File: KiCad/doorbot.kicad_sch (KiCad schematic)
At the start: 54 parts, among them J1 SERVO, J10 Raspberry_Pi_2_3, J2 POWER, J3 SIEDLE LED, J4 SIEDLE KEY, J5 ERT SWITCH, J6 ERT SIEDLE, J7 BUZZER, J8 UI LED, J9 UI BUTTON, Q1 BC337, Q2 BC548, Q3 BC548, U1 PC817, U2 PC817, U3 74HC14, U4 EPR211A064, U5 EPR211A064, U6 L4940, U7 MIC29302WT

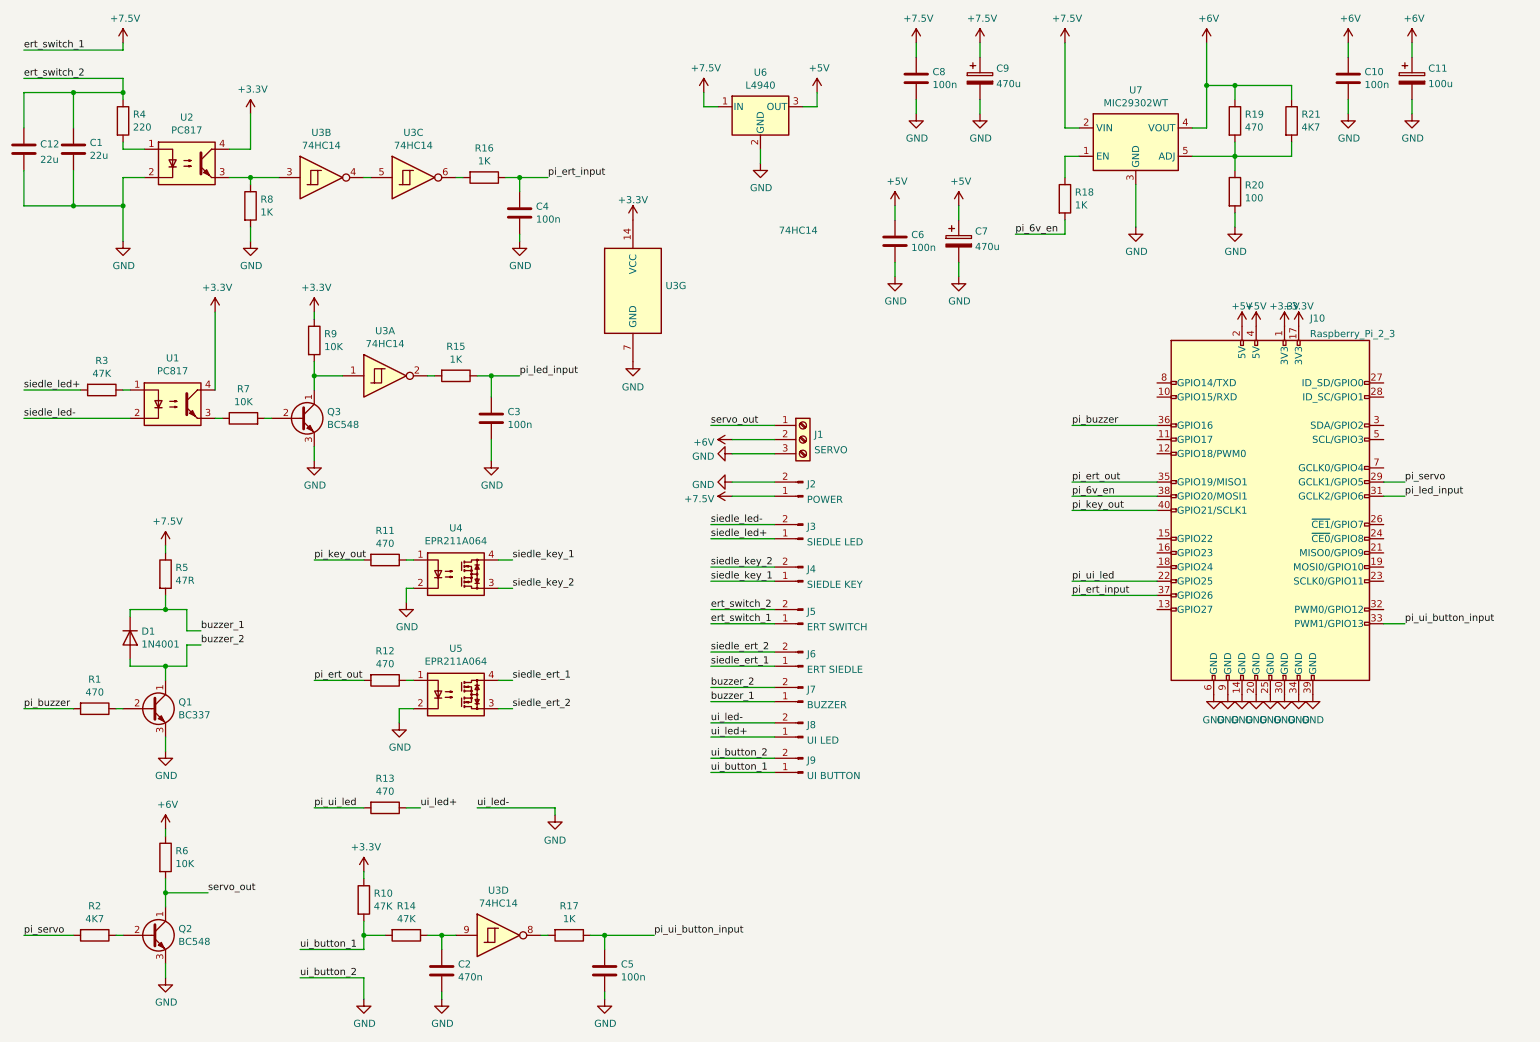
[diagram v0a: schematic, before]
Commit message: Route the stripboard PCB
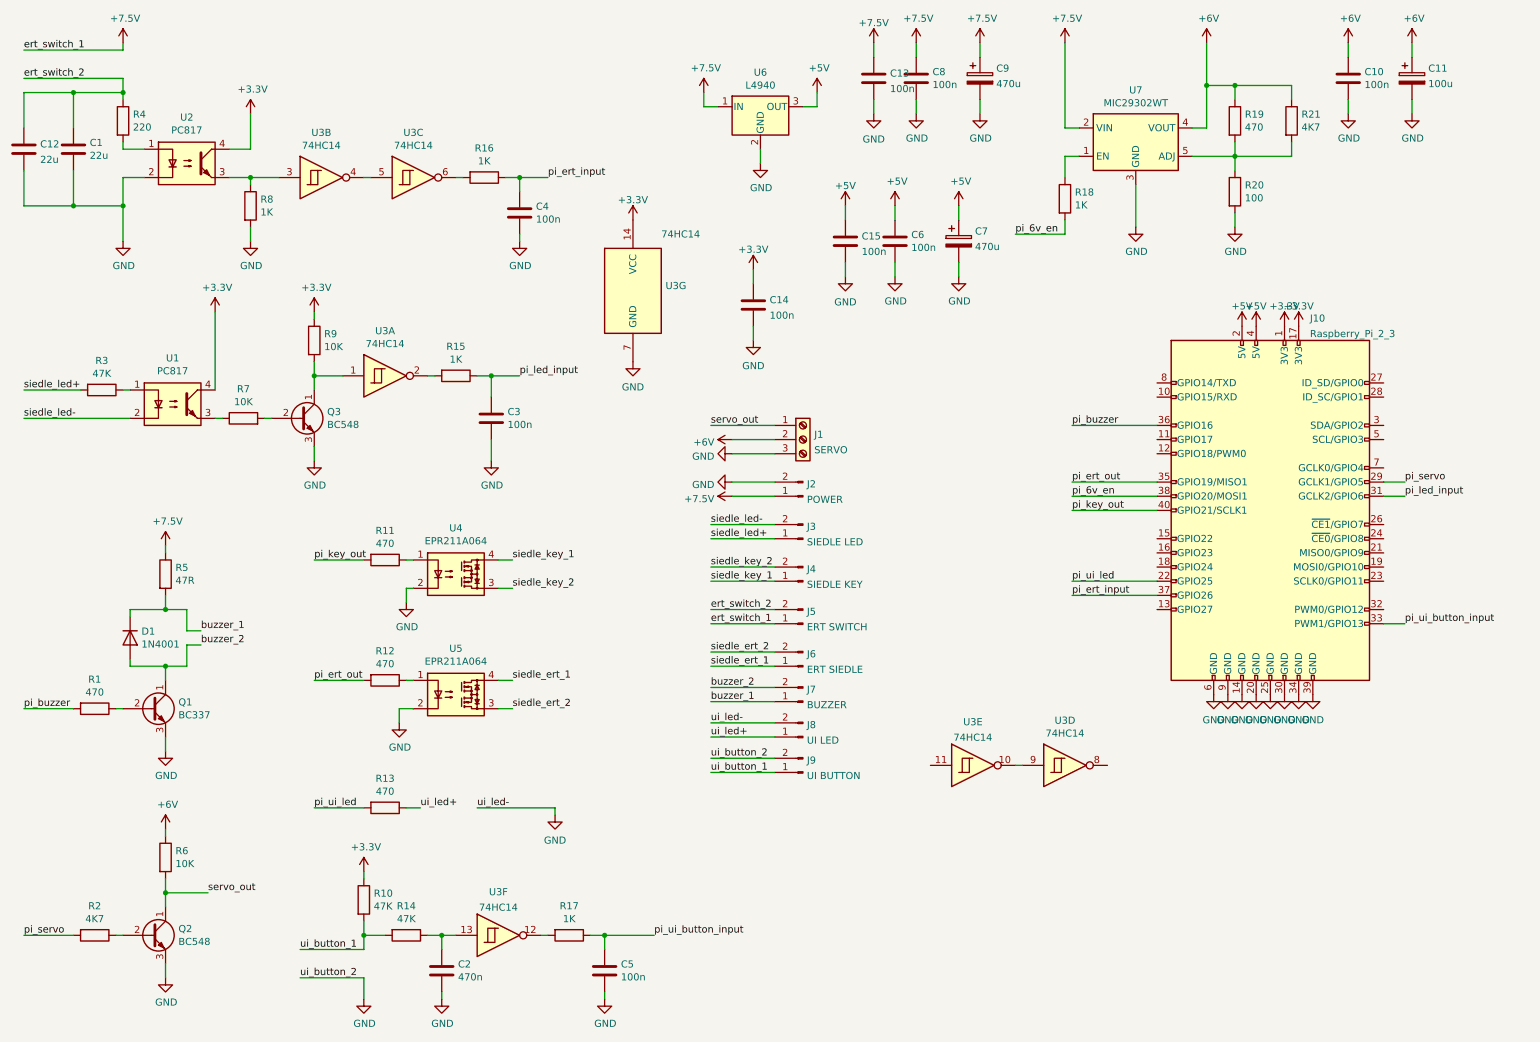
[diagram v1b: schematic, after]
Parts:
- added C13, C14, C15: 100n, Capacitor_THT:C_Disc_D5.0mm_W2.5mm_P2.50mm, symbol Device:C
- added unit 6 of U3
- added unit 5 of U3
- D1: footprint Diode_THT:D_DO-41_SOD81_P10.16mm_Horizontal -> Diode_THT:D_DO-41_SOD81_P2.54mm_Vertical_AnodeUp
- Q1, Q2, Q3: footprint Package_TO_SOT_THT:TO-92_Inline -> Package_TO_SOT_THT:TO-92_Inline_Wide
- R1, R17, R19, R2, R21, R4, R6: footprint Resistor_THT:R_Axial_DIN0207_L6.3mm_D2.5mm_P10.16mm_Horizontal -> Resistor_THT:R_Axial_DIN0207_L6.3mm_D2.5mm_P2.54mm_Vertical
- R10, R15: footprint Resistor_THT:R_Axial_DIN0207_L6.3mm_D2.5mm_P10.16mm_Horizontal -> Resistor_THT:R_Axial_DIN0309_L9.0mm_D3.2mm_P12.70mm_Horizontal
- R11, R13, R14, R18, R20, R3, R5: footprint Resistor_THT:R_Axial_DIN0207_L6.3mm_D2.5mm_P10.16mm_Horizontal -> Resistor_THT:R_Axial_DIN0207_L6.3mm_D2.5mm_P5.08mm_Vertical
- R16: footprint Resistor_THT:R_Axial_DIN0207_L6.3mm_D2.5mm_P10.16mm_Horizontal -> Resistor_THT:R_Axial_DIN0207_L6.3mm_D2.5mm_P15.24mm_Horizontal
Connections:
- net +3V3: now also C14.1
- net +5V: now also C15.1
- net +7.5V: now also C13.1
- net GND: now also C13.2, C14.2, C15.2
- net at C2.1, R14.1: now also U3.13; no longer U3.9
- net at U3.8: no longer R17.2
- new net: U3.10, U3.9
- new net: R17.2, U3.12
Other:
- moved on the sheet: U3D

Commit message: Add the final PCB version
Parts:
- added FB1: Bead, Resistor_THT:R_Axial_DIN0207_L6.3mm_D2.5mm_P10.16mm_Horizontal, symbol Device:FerriteBead
- C12: renamed from C7; value 470u -> 2200u 10V
- C13: renamed from C9; value 470u -> 1000u 16V
- C7: renamed from C14; footprint Capacitor_THT:C_Disc_D5.0mm_W2.5mm_P2.50mm -> Capacitor_THT:C_Disc_D7.5mm_W5.0mm_P7.50mm
- renumbered C12 to C1, C6 to C10, C8 to C11, C10 to C14, C11 to C15, C1 to C2, C2 to C3, C3 to C4, C4 to C5, C5 to C6, C15 to C8, C13 to C9
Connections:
- net +5V: now also FB1.1; no longer C10.1, J10.2 (5V), J10.4 (5V)
- new net: C10.1, FB1.2, J10.2 (5V), J10.4 (5V)
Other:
- moved on the sheet: C10, U6
